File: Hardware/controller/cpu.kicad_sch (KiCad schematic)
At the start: 23 parts

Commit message: Replaced most passives with 0603 size
- This is more compact, and we might as well since this board will be at
  least partially assembled beforehand
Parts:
- R: MPN WR08X101 JTL -> (none)
- U: MPN CL21B104KACNFNC -> (none)
- U: MPN CR0805-JW-102ELF -> (none)
- U: MPN RMC1/10-103JTP -> (none)
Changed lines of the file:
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@@
       (effects (font (size 1.27 1.27)) hide)
     )
-    (property "MPN" "CL21B104KACNFNC" (id 4) (at 58.42 142.875 0)
+    (property "MPN" "" (id 4) (at 58.42 142.875 0)
       (effects (font (size 1.27 1.27)) hide)
     )
@@
       (effects (font (size 1.27 1.27)) hide)
     )
-    (property "MPN" "CR0805-JW-102ELF" (id 4) (at 137.16 183.515 0)
+    (property "MPN" "" (id 4) (at 137.16 183.515 0)
       (effects (font (size 1.27 1.27)) hide)
     )
@@
       (effects (font (size 1.27 1.27)) hide)
     )
-    (property "MPN" "CR0805-JW-102ELF" (id 4) (at 99.06 180.975 0)
+    (property "MPN" "" (id 4) (at 99.06 180.975 0)
       (effects (font (size 1.27 1.27)) hide)
     )
@@
       (effects (font (size 1.27 1.27)) hide)
     )
-    (property "MPN" "CR0805-JW-102ELF" (id 4) (at 165.1 188.595 0)
+    (property "MPN" "" (id 4) (at 165.1 188.595 0)
       (effects (font (size 1.27 1.27)) hide)
     )
@@
       (effects (font (size 1.27 1.27)) hide)
     )
-    (property "MPN" "CR0805-JW-102ELF" (id 4) (at 99.06 191.135 0)
+    (property "MPN" "" (id 4) (at 99.06 191.135 0)
       (effects (font (size 1.27 1.27)) hide)
     )
@@
       (effects (font (size 1.27 1.27)) hide)
     )
-    (property "MPN" "WR08X101 JTL" (id 4) (at 36.83 139.065 90)
+    (property "MPN" "" (id 4) (at 36.83 139.065 90)
       (effects (font (size 1.27 1.27)) hide)
     )
@@
       (effects (font (size 1.27 1.27)) hide)
     )
-    (property "MPN" "CL21B104KACNFNC" (id 4) (at 19.05 160.655 0)
+    (property "MPN" "" (id 4) (at 19.05 160.655 0)
       (effects (font (size 1.27 1.27)) hide)
     )
@@
       (effects (font (size 1.27 1.27)) hide)
     )
-    (property "MPN" "CR0805-JW-102ELF" (id 4) (at 240.665 129.54 0)
+    (property "MPN" "" (id 4) (at 240.665 129.54 0)
       (effects (font (size 1.27 1.27)) hide)
     )
@@
       (effects (font (size 1.27 1.27)) hide)
     )
-    (property "MPN" "RMC1/10-103JTP" (id 4) (at 253.365 129.54 0)
+    (property "MPN" "" (id 4) (at 253.365 129.54 0)
       (effects (font (size 1.27 1.27)) hide)
     )
@@
       (effects (font (size 1.27 1.27)) hide)
     )
-    (property "MPN" "CR0805-JW-102ELF" (id 4) (at 99.06 186.055 0)
-      (effects (font (size 1.27 1.27)) hide)
-    )
+    (property "MPN" "" (id 4) (at 99.06 186.055 0)
+      (effects (font (size 1.27 1.27)) hide)
+    )

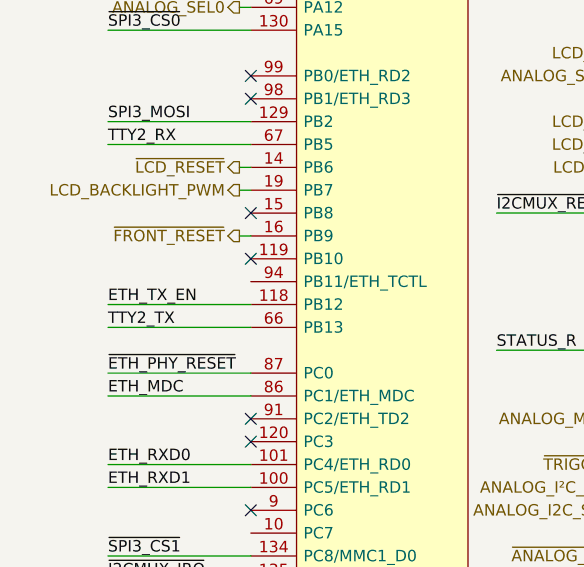
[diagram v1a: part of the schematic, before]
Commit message: Routed Ethernet PHY
- Finished routing the RMII lines to the Ethernet PHY, all of its power
  stuff, and routing its output signals to the Ethernet magjack on the
  side of the board

  This probably needs some revisiting re: the LAN8720 reference
  schematics and layouts
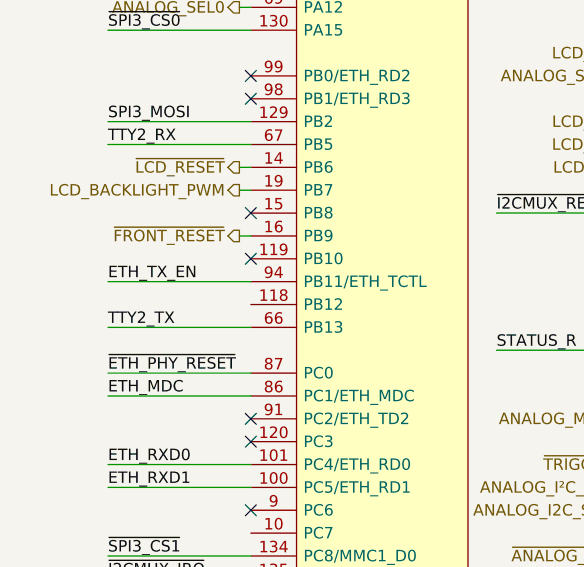
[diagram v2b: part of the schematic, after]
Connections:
- net ETH_TX_EN: now also U.94 (PB11/ETH_TCTL); no longer U.118 (PB12)
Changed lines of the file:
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@@
     (stroke (width 0) (type default))
   )
-  (wire (pts (xy 21.59 77.47) (xy 37.465 77.47))
+  (wire (pts (xy 21.59 74.93) (xy 37.465 74.93))
     (stroke (width 0) (type default))
   )
@@
     (effects (font (size 1.27 1.27)) (justify left bottom))
   )
-  (label "ETH_TX_EN" (at 21.59 77.47 0) (fields_autoplaced)
-    (effects (font (size 1.27 1.27)) (justify left bottom))
-  )
+  (label "ETH_TX_EN" (at 21.59 74.93 0) (fields_autoplaced)
+    (effects (font (size 1.27 1.27)) (justify left bottom))
+  )

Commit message: Auxiliary I2C + SPI bus routing
- Added an I2C MAC EEPROM to the aux I2C bus, which will be read for the
  device serial and Ethernet MAC address

- Add fan controller, filtering/ESD and fusing for expansion connector
  for rear IO section. We'll still have to add the CAN termination as
  well as the CAN transceiver on that part

- Minor routing + pin location tweaks
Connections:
- net ~{I2CMUX_IRQ}: now also U.97 (PA1/ETH_RCLK); no longer U.135 (PC9/MMC1_D1)
- net ~{SPI3_IRQ}: now also U.138 (PC12/MMC1_CK); no longer U.97 (PA1/ETH_RCLK)
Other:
- sheet Ethernet PHY ports: added I²C_SCL , I²C_SDA; removed none
- note added: "Pins to move: - ~{TRIGGER}"
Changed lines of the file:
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@@
   (no_connect (at 37.465 90.17))
   (no_connect (at 37.465 54.61))
+  (no_connect (at 37.465 107.95))
   (no_connect (at 80.645 115.57))
   (no_connect (at 37.465 92.71))
@@
   (no_connect (at 37.465 100.33))
   (no_connect (at 127 67.31))
-  (no_connect (at 37.465 115.57))
   (no_connect (at 37.465 67.31))
   (wire (pts (xy 79.375 105.41) (xy 80.645 105.41))
@@
     (stroke (width 0) (type default))
   )
-  (wire (pts (xy 21.59 107.95) (xy 37.465 107.95))
+  (wire (pts (xy 21.59 115.57) (xy 37.465 115.57))
     (stroke (width 0) (type default))
   )
@@
     (stroke (width 0) (type default))
   )
+  (wire (pts (xy 239.395 104.14) (xy 255.27 104.14))
+    (stroke (width 0) (type default))
+  )
   (wire (pts (xy 212.725 44.45) (xy 213.995 44.45))
     (stroke (width 0) (type default))
@@
   )
   (wire (pts (xy 198.12 86.36) (xy 213.995 86.36))
+    (stroke (width 0) (type default))
+  )
+  (wire (pts (xy 239.395 106.68) (xy 255.27 106.68))
     (stroke (width 0) (type default))
   )
@@
     (effects (font (size 1.27 1.27)) (justify left bottom))
   )
+  (text "Pins to move:\n- ~{TRIGGER}" (at -12.7 60.325 0)
+    (effects (font (size 1.27 1.27)) (justify left bottom))
+  )
   (text "RTC Backup" (at 16.51 128.27 0)
     (effects (font (size 2.54 2.54)) (justify left bottom))
@@
     (effects (font (size 1.27 1.27)) (justify left bottom))
   )
-  (label "~{SPI3_IRQ}" (at 64.77 21.59 0) (fields_autoplaced)
+  (label "~{SPI3_IRQ}" (at 21.59 115.57 0) (fields_autoplaced)
     (effects (font (size 1.27 1.27)) (justify left bottom))
   )
@@
     (effects (font (size 1.27 1.27)) (justify left bottom))
   )
-  (label "~{I2CMUX_IRQ}" (at 21.59 107.95 0) (fields_autoplaced)
+  (label "~{I2CMUX_IRQ}" (at 64.77 21.59 0) (fields_autoplaced)
     (effects (font (size 1.27 1.27)) (justify left bottom))
   )
@@
     (effects (font (size 1.27 1.27)) (justify left bottom))
   )
+  (label "IO_I2C_SDA" (at 255.27 106.68 0) (fields_autoplaced)
+    (effects (font (size 1.27 1.27)) (justify right bottom))
+  )
   (label "~{ETH_PHY_IRQ}" (at 198.12 88.9 0) (fields_autoplaced)
     (effects (font (size 1.27 1.27)) (justify left bottom))
+  )
+  (label "IO_I2C_SCL" (at 255.27 104.14 0) (fields_autoplaced)
+    (effects (font (size 1.27 1.27)) (justify right bottom))
   )
   (label "ETH_CLK" (at 198.12 83.82 0) (fields_autoplaced)
@@
       (effects (font (size 1.27 1.27)) (justify left))
     )
-  )
+    (pin "I²C_SCL " input (at 239.395 104.14 0)
+      (effects (font (size 1.27 1.27)) (justify right))
+    )
+    (pin "I²C_SDA" bidirectional (at 239.395 106.68 0)
+      (effects (font (size 1.27 1.27)) (justify right))
+    )
+  )

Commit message: More controller board routing
- Added components for trigger input (except for the input connector,
  which will need to be some form of terminal)

- Routed more of the power stuff for the expansion/rear IO area, and
  added a relay to control the +12V power output provided on the
  expansion terminals

- Add a zero crossing detector circuit

- Routed status LEDs for controller and control lines for expansion
  (termination and power enable)
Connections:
- net STATUS_B: no longer U.136 (PC10/MMC1_D2)
- net STATUS_R: now also U.136 (PC10/MMC1_D2)
- net EXP_PWR_EN: now reaches U.118 (PB12)
- net CAN_TERM_EN: now reaches U.66 (PB13)
- net ZERO_CROSS: now reaches U.86 (PC1/ETH_MDC)
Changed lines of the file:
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@@
+    (stroke (width 0) (type default))
+  )
+  (wire (pts (xy 79.375 80.01) (xy 80.645 80.01))
     (stroke (width 0) (type default))
   )
@@
     (stroke (width 0) (type default))
   )
+  (wire (pts (xy 79.375 77.47) (xy 80.645 77.47))
+    (stroke (width 0) (type default))
+  )
   (wire (pts (xy 21.59 97.79) (xy 37.465 97.79))
     (stroke (width 0) (type default))
@@
   )
   (wire (pts (xy 239.395 91.44) (xy 240.665 91.44))
+    (stroke (width 0) (type default))
+  )
+  (wire (pts (xy 79.375 87.63) (xy 80.645 87.63))
     (stroke (width 0) (type default))
   )
@@
     (effects (font (size 1.27 1.27)) (justify left bottom))
   )
-  (label "STATUS_B" (at 64.77 110.49 0) (fields_autoplaced)
+  (label "STATUS_R" (at 64.77 110.49 0) (fields_autoplaced)
     (effects (font (size 1.27 1.27)) (justify left bottom))
   )
@@
     (effects (font (size 1.27 1.27)) (justify left bottom))
   )
-  (label "STATUS_R" (at 64.77 82.55 0) (fields_autoplaced)
+  (label "STATUS_B" (at 64.77 82.55 0) (fields_autoplaced)
     (effects (font (size 1.27 1.27)) (justify left bottom))
   )
@@
     (effects (font (size 1.27 1.27)) (justify right))
   )
+  (hierarchical_label "EXP_PWR_EN" (shape output) (at 79.375 77.47 180) (fields_autoplaced)
+    (effects (font (size 1.27 1.27)) (justify right))
+  )
   (hierarchical_label "LCD_G6" (shape output) (at 125.73 62.23 180) (fields_autoplaced)
     (effects (font (size 1.27 1.27)) (justify right))
@@
     (effects (font (size 1.27 1.27)) (justify left))
   )
+  (hierarchical_label "CAN_TERM_EN" (shape output) (at 79.375 80.01 180) (fields_autoplaced)
+    (effects (font (size 1.27 1.27)) (justify right))
+  )
   (hierarchical_label "LCD_SPI_MISO" (shape input) (at 212.725 73.66 180) (fields_autoplaced)
     (effects (font (size 1.27 1.27)) (justify right))
@@
     (effects (font (size 1.27 1.27)) (justify right))
   )
+  (hierarchical_label "ZERO_CROSS" (shape input) (at 79.375 87.63 180) (fields_autoplaced)
+    (effects (font (size 1.27 1.27)) (justify right))
+  )

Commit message: Added triggering circuit
- Routed the trigger circuit for the front panel trigger input

- Replaced magnetic transducer (beeper) with the old up-firing type,
  rather than the side firing type, and moved it since its location
  isn't really that critical

- Added a slightly larger cutout at the front for the input jacks

o#
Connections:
- net ~{TRIGGER}: now also U.138 (PC12/MMC1_CK); no longer U.101 (PC4/ETH_RD0)
- no-connect marks 18 -> 21

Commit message: Add CAN controller, power switch
- Add the schematic sheet for the CAN bus controller (MCP2515) and
  routed all of its signals, including a CAN transceiver and the
  associated SPI lines for the controller

  (tbh ideally we'd use the CAN inside the STM32 but the STM32MP151 in
  the SoM doesn't have that…)

- Added footprint for the NE1838EE mains power switch and started
  routing part of it

- Various tweaks to controller layout
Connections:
- net ~{CAN_RESET}: now reaches U.87 (PC0)
- no-connect marks 21 -> 20
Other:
- added sheet Expansion CAN Controller (canbus.kicad_sch)
- sheet Bus Multiplexers ports: added IO_SPI_MISO, IO_SPI_MOSI, IO_SPI_SCK, ~{IO_SPI_CS}; removed none
- note removed: "CANbus (from CAN controller on SPI3)"
- note removed: "Pins to move: - ~{TRIGGER}"
- note removed: "TODO: Boot mode DIP switch"
- note removed: "TODO: pull-ups for analog I2C bus"
- moved on the sheet: U

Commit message: Finished routing front panel
- Finished routing the contents of the front panel; it could probably
  use an optimization pass and general cleanup.

  A few of the assignments of IOs/LED driver outputs were changed as
  well to make the routing less of a pain in the ass, as compared to the
  previous front panels.

- Minor tweaks to controller to remove some unused signals
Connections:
- net ~{LCD_RESET}: no longer names the net of U.14 (PB6)
- no-connect marks 20 -> 21
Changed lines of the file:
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@@
   (no_connect (at 213.995 127))
   (no_connect (at 162.56 135.255))
+  (no_connect (at 37.465 62.23))
   (no_connect (at 37.465 90.17))
   (no_connect (at 80.645 107.95))
@@
     (stroke (width 0) (type default))
   )
-  (wire (pts (xy 36.195 62.23) (xy 37.465 62.23))
-    (stroke (width 0) (type default))
-  )
   (wire (pts (xy 125.73 77.47) (xy 127 77.47))
     (stroke (width 0) (type default))
@@
     (effects (font (size 1.27 1.27)) (justify right))
   )
-  (hierarchical_label "~{LCD_RESET}" (shape output) (at 36.195 62.23 180) (fields_autoplaced)
-    (effects (font (size 1.27 1.27)) (justify right))
-  )

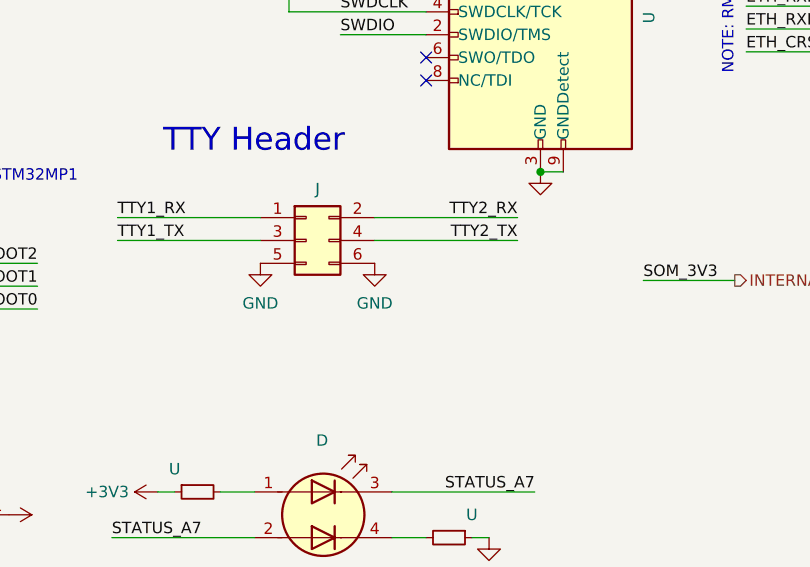
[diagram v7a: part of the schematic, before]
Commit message: Route mains traces on controller board
- Connected the transformer to a wire terminal for the voltage
  switch/input jack as well as the power switch
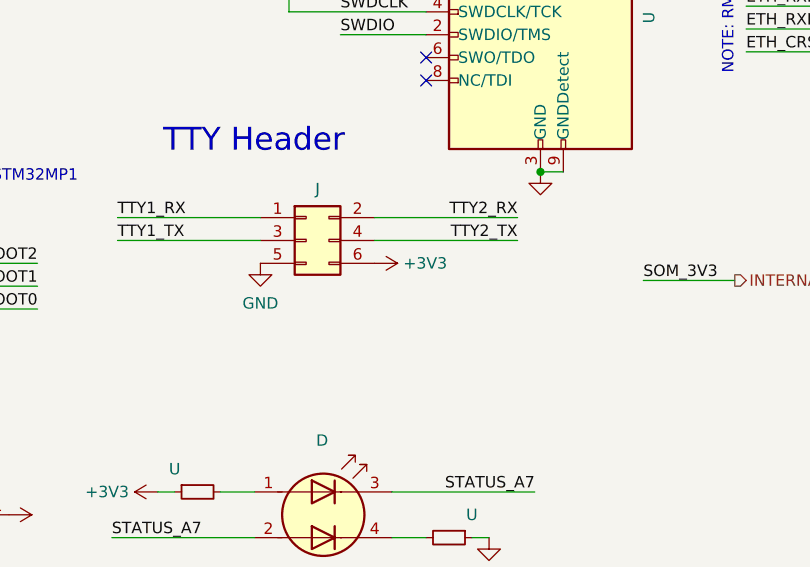
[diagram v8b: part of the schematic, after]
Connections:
- net +3V3: now also J.6 (Pin_6)
- net GND: no longer J.6 (Pin_6)
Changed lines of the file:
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@@
     (pin "4")
+  )
+  (symbol (lib_id "power:+3V3") (at 156.845 158.115 270) (unit 1)
+    (in_bom yes) (on_board yes)
+    (default_instance (reference "#PWR") (unit 1) (value "+3V3") (footprint ""))
+    (property "Reference" "#PWR" (id 0) (at 153.035 158.115 0)
+      (effects (font (size 1.27 1.27)) hide)
+    )
+    (property "Value" "+3V3" (id 1) (at 160.02 158.115 90)
+      (effects (font (size 1.27 1.27)) (justify left))
+    )
+    (property "Footprint" "" (id 2) (at 156.845 158.115 0)
+      (effects (font (size 1.27 1.27)) hide)
+    )
+    (property "Datasheet" "" (id 3) (at 156.845 158.115 0)
+      (effects (font (size 1.27 1.27)) hide)
+    )
+    (pin "1")
   )
   (symbol (lib_id "power:+BATT") (at 58.42 139.065 0) (unit 1)
@@
     (pin "3")
   )
-  (symbol (lib_id "power:GND") (at 156.845 158.115 0) (unit 1)
-    (in_bom yes) (on_board yes) (fields_autoplaced)
-    (default_instance (reference "#PWR") (unit 1) (value "GND") (footprint ""))
-    (property "Reference" "#PWR" (id 0) (at 156.845 164.465 0)
-      (effects (font (size 1.27 1.27)) hide)
-    )
-    (property "Value" "GND" (id 1) (at 156.845 162.56 0)
-      (effects (font (size 1.27 1.27)))
-    )
-    (property "Footprint" "" (id 2) (at 156.845 158.115 0)
-      (effects (font (size 1.27 1.27)) hide)
-    )
-    (property "Datasheet" "" (id 3) (at 156.845 158.115 0)
-      (effects (font (size 1.27 1.27)) hide)
-    )
-    (pin "1")
-  )
   (symbol (lib_id "power:+5V") (at 31.75 177.8 90) (unit 1)
